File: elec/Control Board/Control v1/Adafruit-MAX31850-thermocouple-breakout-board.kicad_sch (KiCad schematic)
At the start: 13 parts

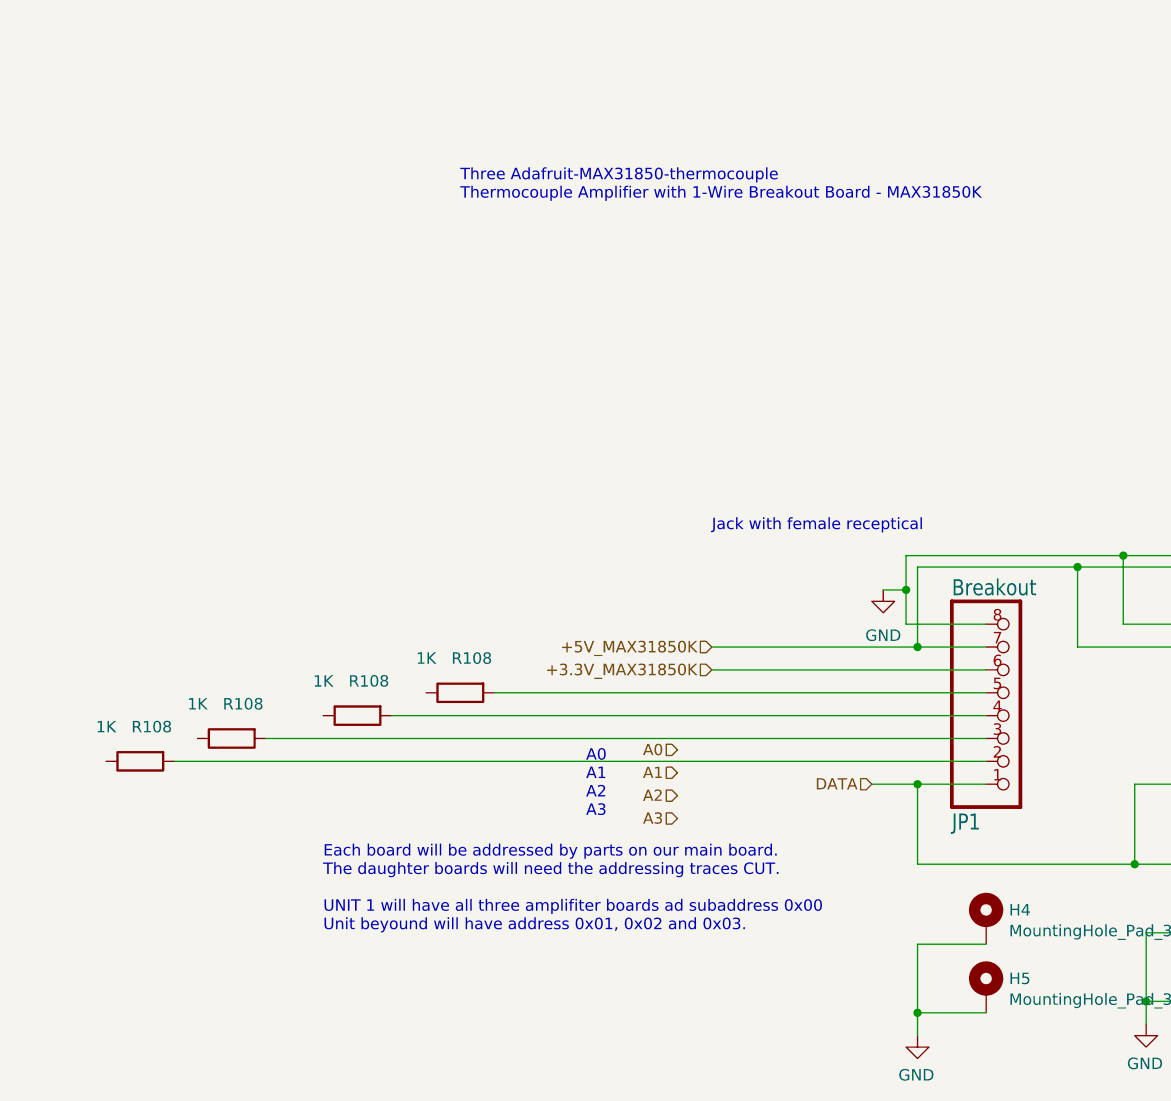
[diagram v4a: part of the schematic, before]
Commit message: Add footrpint to Max31850 module.
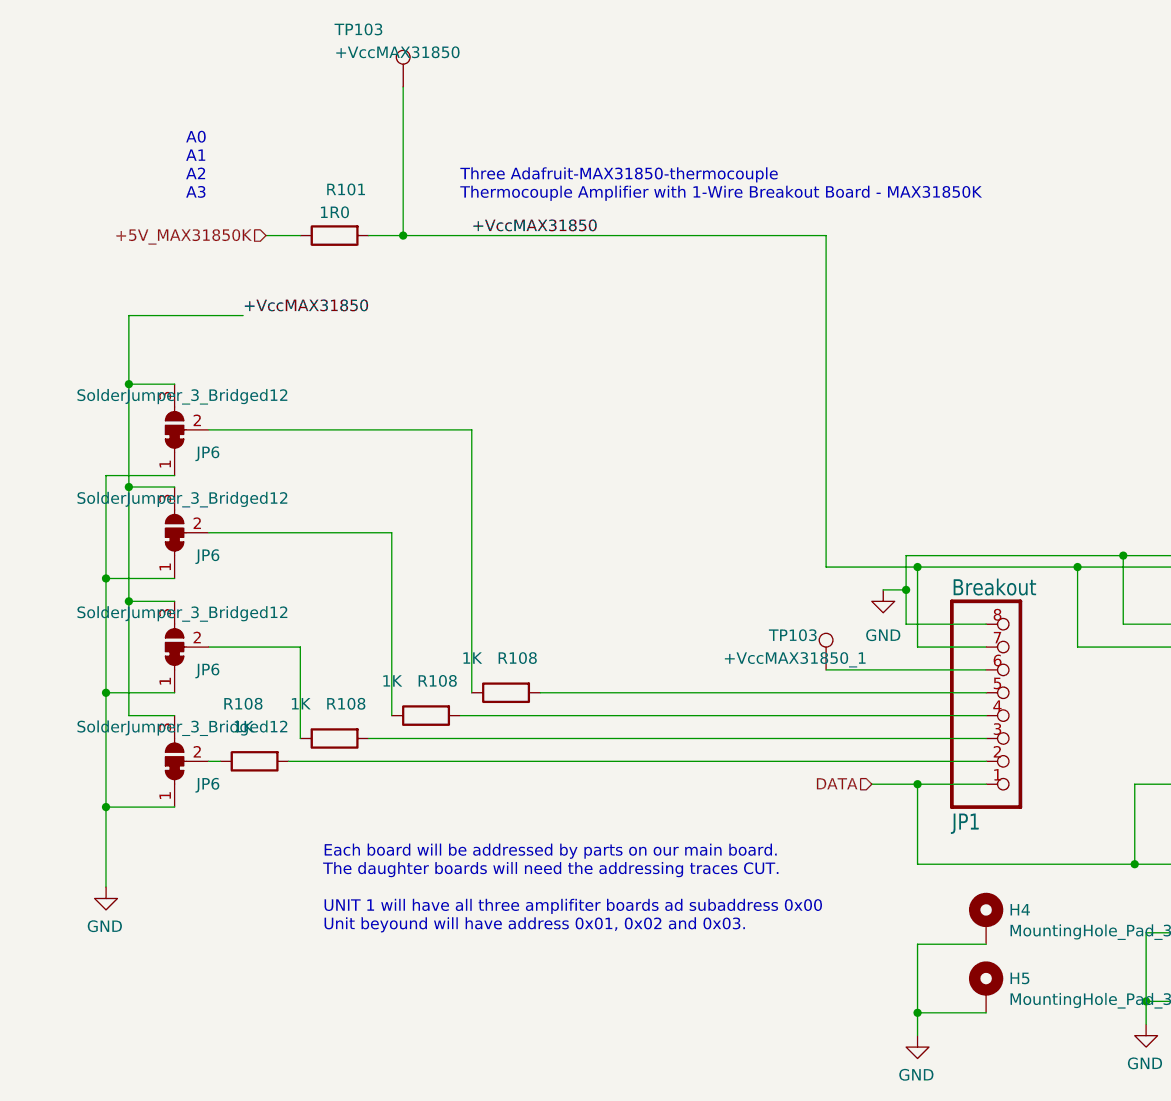
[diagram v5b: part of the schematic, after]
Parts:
- added JP6 (x4): SolderJumper_3_Bridged12, Jumper:SolderJumper-3_P1.3mm_Bridged12_RoundedPad1.0x1.5mm, symbol Jumper:SolderJumper_3_Bridged12
- added R101: 1R0, Resistor_SMD:R_0603_1608Metric_Pad0.98x0.95mm_HandSolder, symbol Device:R
- added TP103: +VccMAX31850, TestPoint:TestPoint_Loop_D2.54mm_Drill1.5mm_Beaded, symbol Connector:TestPoint
- added TP103: +VccMAX31850_1, TestPoint:TestPoint_Loop_D2.54mm_Drill1.5mm_Beaded, symbol Connector:TestPoint
- JP1, JP2, JP3: footprint Control v1:1X08_ROUND_70 -> PubInv_KiCad_PCB:Adafruit_MAX31850K_Module
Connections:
- net +5V_MAX31850K: now also R101.1; no longer JP1.7, JP2.7, JP3.7
- net GND: now also JP6.1 (A), JP6.1 (A), JP6.1 (A), JP6.1 (A)
- net at R108.1: now also JP6.2 (C) (x4)
- net +3.3V_MAX31850K: no longer names the net of JP1.6
- net +3.3V_MAX31850K: now also TP103.1
- new net +VccMAX31850: JP1.7, JP2.7, JP3.7, JP6.3 (B), JP6.3 (B), JP6.3 (B), JP6.3 (B), R101.2, TP103.1
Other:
- note removed: "Jack with female receptical"
- moved on the sheet: R108

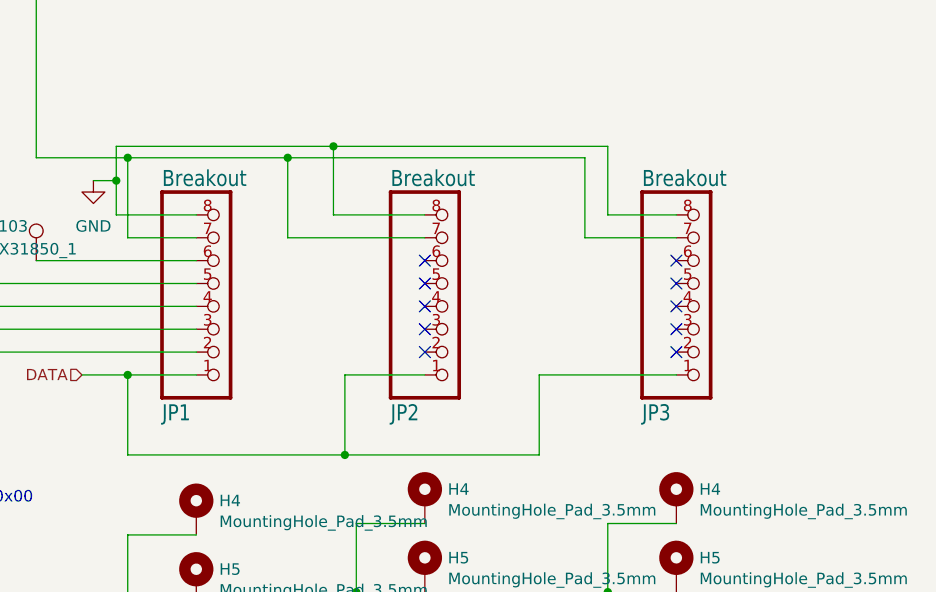
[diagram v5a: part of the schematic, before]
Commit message: Add footprints for thermoucouple modules to schematic and PCB.  This commit does NOT capture the library changes.
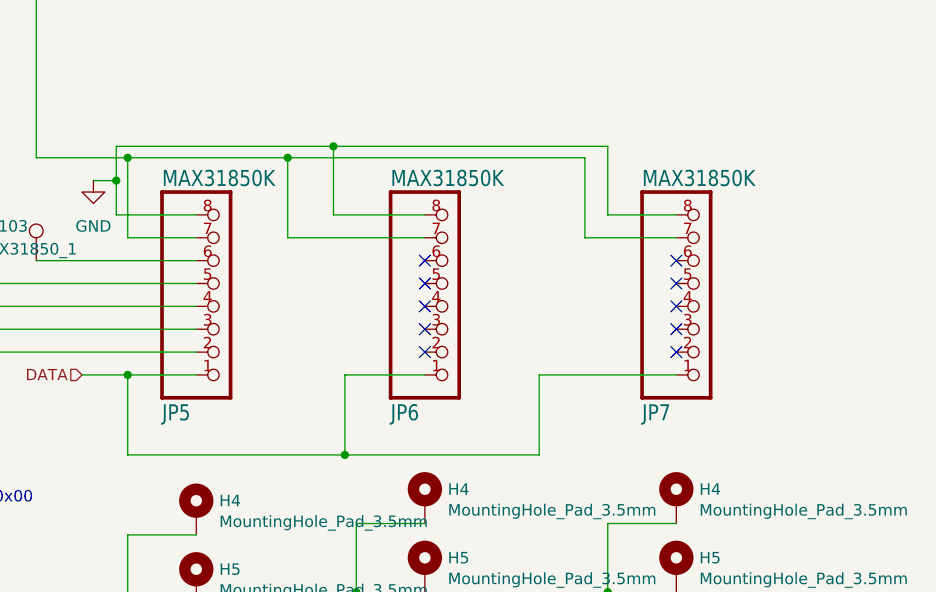
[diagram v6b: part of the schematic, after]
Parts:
- JP5: renamed from JP1; value Breakout -> MAX31850K
- JP6: renamed from JP2; value Breakout -> MAX31850K
- JP7: renamed from JP3; value Breakout -> MAX31850K
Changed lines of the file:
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@@
   (symbol (lib_id "Control v1-eagle-import:microbuilder_HEADER-1X870MIL") (at 135.89 91.44 0) (mirror x) (unit 1)
     (in_bom yes) (on_board yes) (dnp no)
-    (property "Reference" "JP2" (at 129.54 104.775 0)
+    (property "Reference" "JP6" (at 129.54 104.775 0)
       (effects (font (size 1.778 1.5113)) (justify left bottom))
     )
-    (property "Value" "Breakout" (at 129.54 78.74 0)
+    (property "Value" "MAX31850K" (at 129.54 78.74 0)
       (effects (font (size 1.778 1.5113)) (justify left bottom))
     )
@@
       (project "Control v1"
         (path "/c68c9deb-8d4d-42f0-adf8-4d3022f4ee59/3ff32a52-b1ed-4756-8661-90a95f721605"
-          (reference "JP2") (unit 1)
+          (reference "JP6") (unit 1)
         )
       )
@@
         )
         (path "/c68c9deb-8d4d-42f0-adf8-4d3022f4ee59/3ff32a52-b1ed-4756-8661-90a95f721605"
-          (reference "JP9") (unit 1)
+          (reference "JP4") (unit 1)
         )
       )
@@
         )
         (path "/c68c9deb-8d4d-42f0-adf8-4d3022f4ee59/3ff32a52-b1ed-4756-8661-90a95f721605"
-          (reference "JP7") (unit 1)
+          (reference "JP2") (unit 1)
         )
       )
@@
         )
         (path "/c68c9deb-8d4d-42f0-adf8-4d3022f4ee59/3ff32a52-b1ed-4756-8661-90a95f721605"
-          (reference "R9") (unit 1)
+          (reference "R10") (unit 1)
         )
       )
@@
         )
         (path "/c68c9deb-8d4d-42f0-adf8-4d3022f4ee59/3ff32a52-b1ed-4756-8661-90a95f721605"
-          (reference "JP8") (unit 1)
+          (reference "JP1") (unit 1)
         )
       )
@@
   (symbol (lib_id "Control v1-eagle-import:microbuilder_HEADER-1X870MIL") (at 110.49 91.44 0) (mirror x) (unit 1)
     (in_bom yes) (on_board yes) (dnp no)
-    (property "Reference" "JP1" (at 104.14 104.775 0)
+    (property "Reference" "JP5" (at 104.14 104.775 0)
       (effects (font (size 1.778 1.5113)) (justify left bottom))
     )
-    (property "Value" "Breakout" (at 104.14 78.74 0)
+    (property "Value" "MAX31850K" (at 104.14 78.74 0)
       (effects (font (size 1.778 1.5113)) (justify left bottom))
     )
@@
       (project "Control v1"
         (path "/c68c9deb-8d4d-42f0-adf8-4d3022f4ee59/3ff32a52-b1ed-4756-8661-90a95f721605"
-          (reference "JP1") (unit 1)
+          (reference "JP5") (unit 1)
         )
       )
@@
         )
         (path "/c68c9deb-8d4d-42f0-adf8-4d3022f4ee59/3ff32a52-b1ed-4756-8661-90a95f721605"
-          (reference "R10") (unit 1)
+          (reference "R7") (unit 1)
         )
       )
@@
         )
         (path "/c68c9deb-8d4d-42f0-adf8-4d3022f4ee59/3ff32a52-b1ed-4756-8661-90a95f721605"
-          (reference "R8") (unit 1)
+          (reference "R9") (unit 1)
         )
       )
@@
         )
         (path "/c68c9deb-8d4d-42f0-adf8-4d3022f4ee59/3ff32a52-b1ed-4756-8661-90a95f721605"
-          (reference "JP6") (unit 1)
+          (reference "JP3") (unit 1)
         )
       )
@@
       (project "Control v1"
         (path "/c68c9deb-8d4d-42f0-adf8-4d3022f4ee59/3ff32a52-b1ed-4756-8661-90a95f721605"
-          (reference "TP10") (unit 1)
+          (reference "TP2") (unit 1)
         )
       )
@@
   (symbol (lib_id "Control v1-eagle-import:microbuilder_HEADER-1X870MIL") (at 163.83 91.44 0) (mirror x) (unit 1)
     (in_bom yes) (on_board yes) (dnp no)
-    (property "Reference" "JP3" (at 157.48 104.775 0)
+    (property "Reference" "JP7" (at 157.48 104.775 0)
       (effects (font (size 1.778 1.5113)) (justify left bottom))
     )
-    (property "Value" "Breakout" (at 157.48 78.74 0)
+    (property "Value" "MAX31850K" (at 157.48 78.74 0)
       (effects (font (size 1.778 1.5113)) (justify left bottom))
     )
@@
       (project "Control v1"
         (path "/c68c9deb-8d4d-42f0-adf8-4d3022f4ee59/3ff32a52-b1ed-4756-8661-90a95f721605"
-          (reference "JP3") (unit 1)
+          (reference "JP7") (unit 1)
         )
       )
@@
         )
         (path "/c68c9deb-8d4d-42f0-adf8-4d3022f4ee59/3ff32a52-b1ed-4756-8661-90a95f721605"
-          (reference "R7") (unit 1)
-        )
-      )
+          (reference "R8") (unit 1)
+        )
+      )

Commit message: Fix mounting holes for thermocouple.
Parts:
- H4, H5: footprint GeneralPurposeAlarmDevicePCB:MountingHole_3.5mm_Pad_Via -> PubInv_KiCad_PCB:MountingHole_3.5mm_Pad_Via
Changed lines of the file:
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@@
       (effects (font (size 1.27 1.27)) (justify left))
     )
-    (property "Footprint" "GeneralPurposeAlarmDevicePCB:MountingHole_3.5mm_Pad_Via" (at 161.29 115.57 0)
+    (property "Footprint" "PubInv_KiCad_PCB:MountingHole_3.5mm_Pad_Via" (at 161.29 115.57 0)
       (effects (font (size 1.27 1.27)) hide)
     )
@@
       (effects (font (size 1.27 1.27)) (justify left))
     )
-    (property "Footprint" "GeneralPurposeAlarmDevicePCB:MountingHole_3.5mm_Pad_Via" (at 161.29 123.19 0)
+    (property "Footprint" "PubInv_KiCad_PCB:MountingHole_3.5mm_Pad_Via" (at 161.29 123.19 0)
       (effects (font (size 1.27 1.27)) hide)
     )
@@
       (effects (font (size 1.27 1.27)) (justify left))
     )
-    (property "Footprint" "GeneralPurposeAlarmDevicePCB:MountingHole_3.5mm_Pad_Via" (at 107.95 116.84 0)
+    (property "Footprint" "PubInv_KiCad_PCB:MountingHole_3.5mm_Pad_Via" (at 107.95 116.84 0)
       (effects (font (size 1.27 1.27)) hide)
     )
@@
       (effects (font (size 1.27 1.27)) (justify left))
     )
-    (property "Footprint" "GeneralPurposeAlarmDevicePCB:MountingHole_3.5mm_Pad_Via" (at 107.95 124.46 0)
+    (property "Footprint" "PubInv_KiCad_PCB:MountingHole_3.5mm_Pad_Via" (at 107.95 124.46 0)
       (effects (font (size 1.27 1.27)) hide)
     )
@@
       (effects (font (size 1.27 1.27)) (justify left))
     )
-    (property "Footprint" "GeneralPurposeAlarmDevicePCB:MountingHole_3.5mm_Pad_Via" (at 133.35 115.57 0)
+    (property "Footprint" "PubInv_KiCad_PCB:MountingHole_3.5mm_Pad_Via" (at 133.35 115.57 0)
       (effects (font (size 1.27 1.27)) hide)
     )
@@
       (effects (font (size 1.27 1.27)) (justify left))
     )
-    (property "Footprint" "GeneralPurposeAlarmDevicePCB:MountingHole_3.5mm_Pad_Via" (at 133.35 123.19 0)
-      (effects (font (size 1.27 1.27)) hide)
-    )
+    (property "Footprint" "PubInv_KiCad_PCB:MountingHole_3.5mm_Pad_Via" (at 133.35 123.19 0)
+      (effects (font (size 1.27 1.27)) hide)
+    )
